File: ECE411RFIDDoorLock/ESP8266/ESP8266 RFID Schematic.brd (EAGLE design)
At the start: 61 x 43.8 mm, 30 parts, among them M1 SERVO, Q3 DMG341, T1 600mA/40V, T2 600mA/40V, U3 AP2112-3.3, X1 ESP-12E, X4 20329

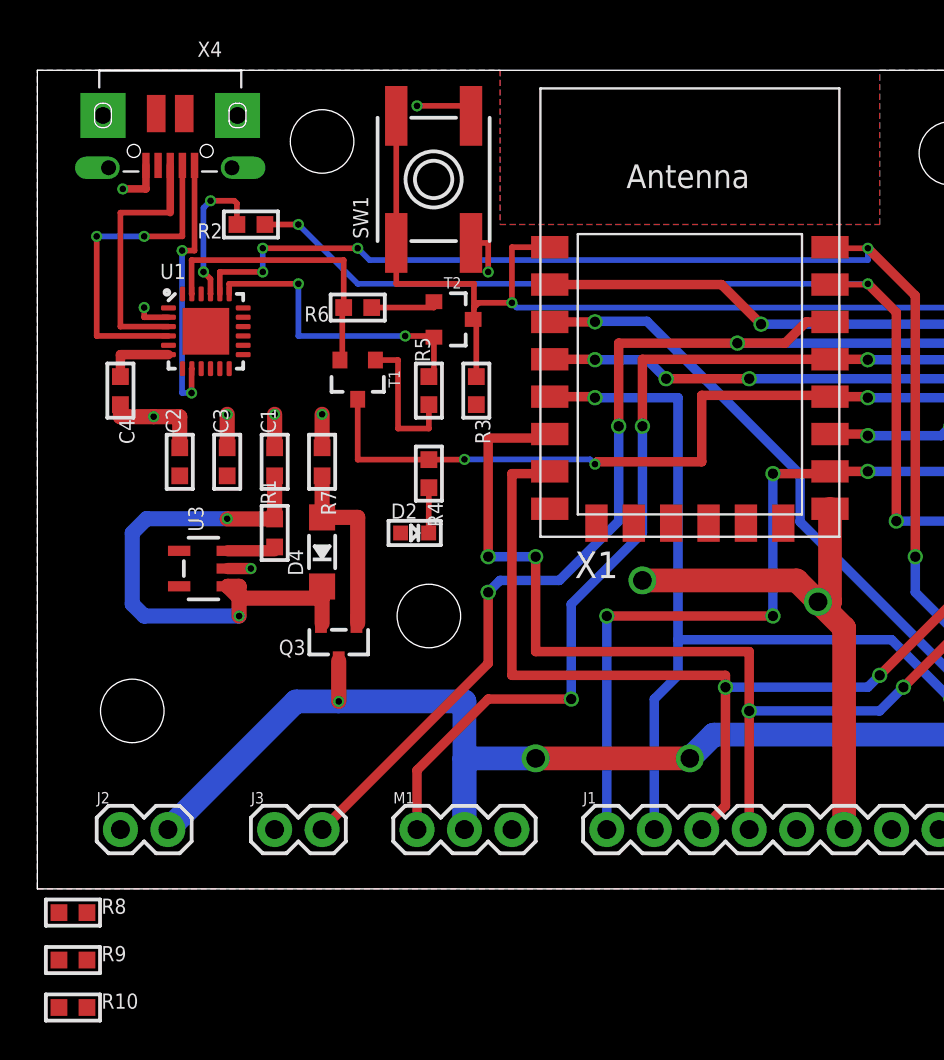
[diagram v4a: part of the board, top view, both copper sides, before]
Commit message: Added and routed resistors R8 - R10 that were missing from original schematic
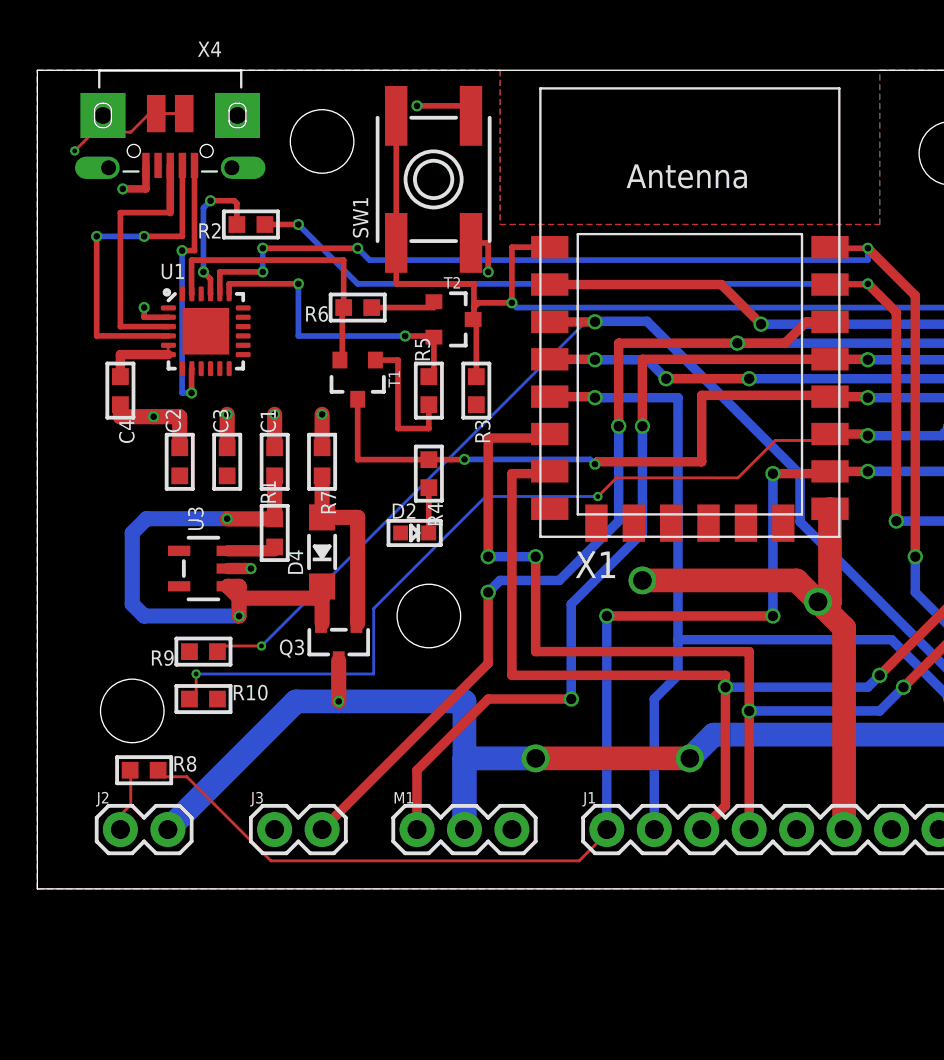
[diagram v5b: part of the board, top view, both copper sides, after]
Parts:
- moved R10 17.9 mm to (8.89, 10.2)
- moved R9 17.9 mm to (8.89, 12.7), turned to 180 degrees
- moved R8 8.52 mm to (5.71, 6.35)
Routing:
- net GPIO2: track 12.3 -> 55.1 mm, vias 2 -> 4
- net CH_PD: track 43.2 -> 70.7 mm, vias 1 -> 2
- net GPIO15: track 44.3 -> 71.3 mm
- net GND: track 50.6 -> 61.1 mm, vias 11 -> 12
- net N$14: track 3.75 -> 4.44 mm
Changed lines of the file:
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@@
 <autorouter>
 <pass name="Default">
-<param name="RoutingGrid" value="50mil"/>
+<param name="RoutingGrid" value="0.125mm"/>
 <param name="AutoGrid" value="1"/>
 <param name="Efforts" value="2"/>
 <param name="TopRouterVariant" value="1"/>
 <param name="tpViaShape" value="round"/>
-<param name="PrefDir.1" value="a"/>
+<param name="PrefDir.1" value="*"/>
 <param name="PrefDir.2" value="0"/>
 <param name="PrefDir.3" value="0"/>
@@
 <param name="PrefDir.14" value="0"/>
 <param name="PrefDir.15" value="0"/>
-<param name="PrefDir.16" value="a"/>
+<param name="PrefDir.16" value="-"/>
 <param name="cfVia" value="8"/>
 <param name="cfNonPref" value="5"/>
@@
 <attribute name="VALUE" x="9.89" y="45.907" size="0.4064" layer="27" ratio="10" rot="R180"/>
 </element>
-<element name="R8" library="microbuilder" package="0603-MINI" value="4.7k" x="1.905" y="-1.27" smashed="yes">
-<attribute name="NAME" x="3.429" y="-1.3335" size="0.8128" layer="25" ratio="18"/>
-<attribute name="VALUE" x="3.429" y="-1.905" size="0.4064" layer="27" ratio="10"/>
-</element>
-<element name="R9" library="microbuilder" package="0603-MINI" value="10k" x="1.905" y="-3.81" smashed="yes">
-<attribute name="NAME" x="3.429" y="-3.8735" size="0.8128" layer="25" ratio="18"/>
-<attribute name="VALUE" x="3.429" y="-4.445" size="0.4064" layer="27" ratio="10"/>
-</element>
-<element name="R10" library="microbuilder" package="0603-MINI" value="10k" x="1.905" y="-6.35" smashed="yes">
-<attribute name="NAME" x="3.429" y="-6.4135" size="0.8128" layer="25" ratio="18"/>
-<attribute name="VALUE" x="3.429" y="-6.985" size="0.4064" layer="27" ratio="10"/>
+<element name="R8" library="microbuilder" package="0603-MINI" value="4.7k" x="5.715" y="6.35" smashed="yes">
+<attribute name="NAME" x="7.239" y="6.2865" size="0.8128" layer="25" ratio="18"/>
+<attribute name="VALUE" x="7.239" y="5.715" size="0.4064" layer="27" ratio="10"/>
+</element>
+<element name="R9" library="microbuilder" package="0603-MINI" value="10k" x="8.89" y="12.7" smashed="yes" rot="R180">
+<attribute name="NAME" x="7.366" y="12.7635" size="0.8128" layer="25" ratio="18" rot="R180"/>
+<attribute name="VALUE" x="7.366" y="13.335" size="0.4064" layer="27" ratio="10" rot="R180"/>
+</element>
+<element name="R10" library="microbuilder" package="0603-MINI" value="10k" x="8.89" y="10.16" smashed="yes">
+<attribute name="NAME" x="10.414" y="10.0965" size="0.8128" layer="25" ratio="18"/>
+<attribute name="VALUE" x="10.414" y="9.525" size="0.4064" layer="27" ratio="10"/>
 </element>
 </elements>
@@
 </polygon>
 <contactref element="R8" pad="1"/>
-<wire x1="42.425" y1="20.345" x2="57.15" y2="33.655" width="0" layer="19" extent="1-1"/>
-<wire x1="25.4" y1="3.175" x2="32.385" y2="16.51" width="0" layer="19" extent="1-1"/>
-<wire x1="12.7" y1="3.175" x2="25.4" y2="3.175" width="0" layer="19" extent="1-1"/>
-<wire x1="4.445" y1="3.175" x2="12.7" y2="3.175" width="0" layer="19" extent="1-1"/>
-<wire x1="1.155" y1="-1.27" x2="4.445" y2="3.175" width="0" layer="19" extent="1-1"/>
-<wire x1="11.43" y1="17.145" x2="12.7" y2="3.175" width="0" layer="19" extent="1-1"/>
-<wire x1="10.16" y1="23.61" x2="10.1901" y2="17.145" width="0" layer="19" extent="1-1"/>
-<wire x1="12.7" y1="25.4" x2="10.16" y2="25.4" width="0" layer="19" extent="1-1"/>
-<wire x1="15.24" y1="25.4" x2="12.7" y2="25.4" width="0" layer="19" extent="1-1"/>
-<wire x1="7.62" y1="23.61" x2="10.16" y2="23.61" width="0" layer="19" extent="1-1"/>
-<wire x1="7.017" y1="30.595" x2="4.445" y2="25.92" width="0" layer="19" extent="1-1"/>
-<wire x1="4.572" y1="37.465" x2="5.715" y2="31.115" width="0" layer="19" extent="1-1"/>
-<wire x1="3.812" y1="38.597" x2="4.572" y2="37.465" width="0" layer="19" extent="1-1"/>
-<wire x1="6.362" y1="41.497" x2="5.812" y2="38.722" width="0" layer="19" extent="1-1"/>
-<wire x1="7.862" y1="41.497" x2="6.362" y2="41.497" width="0" layer="19" extent="1-1"/>
-<wire x1="3.512" y1="41.397" x2="3.812" y2="38.597" width="0" layer="19" extent="1-1"/>
-<wire x1="10.712" y1="41.397" x2="7.862" y2="41.497" width="0" layer="19" extent="1-1"/>
-<wire x1="10.412" y1="38.597" x2="10.712" y2="41.397" width="0" layer="19" extent="1-1"/>
-<wire x1="20.32" y1="41.91" x2="10.712" y2="41.397" width="0" layer="19" extent="1-1"/>
-<wire x1="23.209" y1="34.573" x2="23.209" y2="41.373" width="0" layer="19" extent="1-1"/>
+<wire x1="5" y1="4.5" x2="5" y2="6" width="0.1524" layer="1"/>
+<wire x1="4" y1="3.5" x2="5" y2="4.5" width="0.1524" layer="1"/>
+<wire x1="5" y1="6" x2="4.965" y2="6.35" width="0.1524" layer="1"/>
+<wire x1="4" y1="3.5" x2="4.445" y2="3.175" width="0.1524" layer="1"/>
+<wire x1="3" y1="40.5" x2="2" y2="39.5" width="0.1524" layer="1"/>
+<wire x1="5" y1="40.5" x2="3" y2="40.5" width="0.1524" layer="1"/>
+<wire x1="6" y1="41.5" x2="5" y2="40.5" width="0.1524" layer="1"/>
+<wire x1="6" y1="41.5" x2="6.362" y2="41.497" width="0.1524" layer="1"/>
+<wire x1="6.5" y1="41.5" x2="7.5" y2="41.5" width="0.1524" layer="1"/>
+<wire x1="7.5" y1="41.5" x2="7.862" y2="41.497" width="0.1524" layer="1"/>
+<wire x1="6.5" y1="41.5" x2="6.362" y2="41.497" width="0.1524" layer="1"/>
+<via x="2" y="39.5" extent="1-16" drill="0.254"/>
 </signal>
 <signal name="N$9">
@@
 <wire x1="50.045" y1="22.345" x2="53.975" y2="18.415" width="0.508" layer="16"/>
 <contactref element="R8" pad="2"/>
-<wire x1="2.655" y1="-1.27" x2="30.48" y2="3.175" width="0" layer="19" extent="1-1"/>
+<wire x1="8" y1="6" x2="6.5" y2="6" width="0.1524" layer="1"/>
+<wire x1="12.5" y1="1.5" x2="8" y2="6" width="0.1524" layer="1"/>
+<wire x1="29" y1="1.5" x2="12.5" y2="1.5" width="0.1524" layer="1"/>
+<wire x1="30.5" y1="3" x2="29" y2="1.5" width="0.1524" layer="1"/>
+<wire x1="6.5" y1="6" x2="6.465" y2="6.35" width="0.1524" layer="1"/>
+<wire x1="30.5" y1="3" x2="30.48" y2="3.175" width="0.1524" layer="1"/>
 </signal>
 <signal name="GPIO0">
@@
 <wire x1="50.165" y1="26.035" x2="53.975" y2="26.035" width="0.508" layer="1"/>
 <contactref element="R10" pad="1"/>
-<wire x1="1.155" y1="-6.35" x2="42.425" y2="24.345" width="0" layer="19" extent="1-1"/>
+<wire x1="8.5" y1="11.5" x2="8.5" y2="10.5" width="0.1524" layer="1"/>
+<wire x1="18" y1="11.5" x2="8.5" y2="11.5" width="0.1524" layer="16"/>
+<wire x1="18" y1="15" x2="18" y2="11.5" width="0.1524" layer="16"/>
+<wire x1="24" y1="21" x2="18" y2="15" width="0.1524" layer="16"/>
+<wire x1="30" y1="21" x2="24" y2="21" width="0.1524" layer="16"/>
+<wire x1="31" y1="22" x2="30" y2="21" width="0.1524" layer="1"/>
+<wire x1="37.5" y1="22" x2="31" y2="22" width="0.1524" layer="1"/>
+<wire x1="39.5" y1="24" x2="37.5" y2="22" width="0.1524" layer="1"/>
+<wire x1="42" y1="24" x2="39.5" y2="24" width="0.1524" layer="1"/>
+<wire x1="8.5" y1="10.5" x2="8.14" y2="10.16" width="0.1524" layer="1"/>
+<wire x1="42" y1="24" x2="42.425" y2="24.345" width="0.1524" layer="1"/>
+<via x="8.5" y="11.5" extent="1-16" drill="0.254"/>
+<via x="30" y="21" extent="1-16" drill="0.254"/>
 </signal>
 <signal name="GPIO5/SCL">
@@
 <wire x1="32.6287" y1="30.3784" x2="40.8239" y2="22.1832" width="0.508" layer="16"/>
 <contactref element="R9" pad="1"/>
-<wire x1="1.155" y1="-3.81" x2="27.425" y2="30.345" width="0" layer="19" extent="1-1"/>
+<wire x1="12" y1="13" x2="10" y2="13" width="0.1524" layer="1"/>
+<wire x1="29.5" y1="30.5" x2="12" y2="13" width="0.1524" layer="16"/>
+<wire x1="10" y1="13" x2="9.64" y2="12.7" width="0.1524" layer="1"/>
+<wire x1="29.5" y1="30.5" x2="29.845" y2="30.353" width="0.1524" layer="16"/>
+<via x="12" y="13" extent="1-16" drill="0.254"/>
 </signal>
 <signal name="USB_RX">
@@
 <contactref element="R9" pad="2"/>
 <contactref element="R10" pad="2"/>
-<wire x1="27.425" y1="20.345" x2="57.15" y2="38.735" width="0" layer="19" extent="1-1"/>
-<wire x1="23.495" y1="25.92" x2="27.425" y2="20.345" width="0" layer="19" extent="1-1"/>
-<wire x1="19.443" y1="19.05" x2="23.495" y2="25.92" width="0" layer="19" extent="1-1"/>
-<wire x1="10.16" y1="22.11" x2="19.443" y2="19.05" width="0" layer="19" extent="1-1"/>
-<wire x1="7.62" y1="22.11" x2="10.16" y2="22.11" width="0" layer="19" extent="1-1"/>
-<wire x1="7.767" y1="27.845" x2="7.62" y2="22.11" width="0" layer="19" extent="1-1"/>
-<wire x1="7.5899" y1="16.195" x2="7.62" y2="22.11" width="0" layer="19" extent="1-1"/>
-<wire x1="2.655" y1="-3.81" x2="7.5899" y2="16.195" width="0" layer="19" extent="1-1"/>
-<wire x1="2.655" y1="-6.35" x2="2.655" y2="-3.81" width="0" layer="19" extent="1-1"/>
-<wire x1="48.26" y1="3.175" x2="27.425" y2="20.345" width="0" layer="19" extent="1-1"/>
 </signal>
 <signal name="N$2">
@@
 <wire x1="4.445" y1="27.42" x2="4.445" y2="28.595" width="0.508" layer="1"/>
 <wire x1="4.445" y1="28.595" x2="7.017" y2="28.595" width="0.508" layer="1"/>
-<wire x1="7.017" y1="28.595" x2="7.017" y2="29.095" width="0" layer="19" extent="1-1"/>
+<wire x1="7" y1="28.5" x2="7" y2="29" width="0.1524" layer="1"/>
+<wire x1="7" y1="29" x2="7.017" y2="29.095" width="0.1524" layer="1"/>
+<wire x1="7" y1="28.5" x2="7.017" y2="28.595" width="0.1524" layer="1"/>
 </signal>
 <signal name="EN">

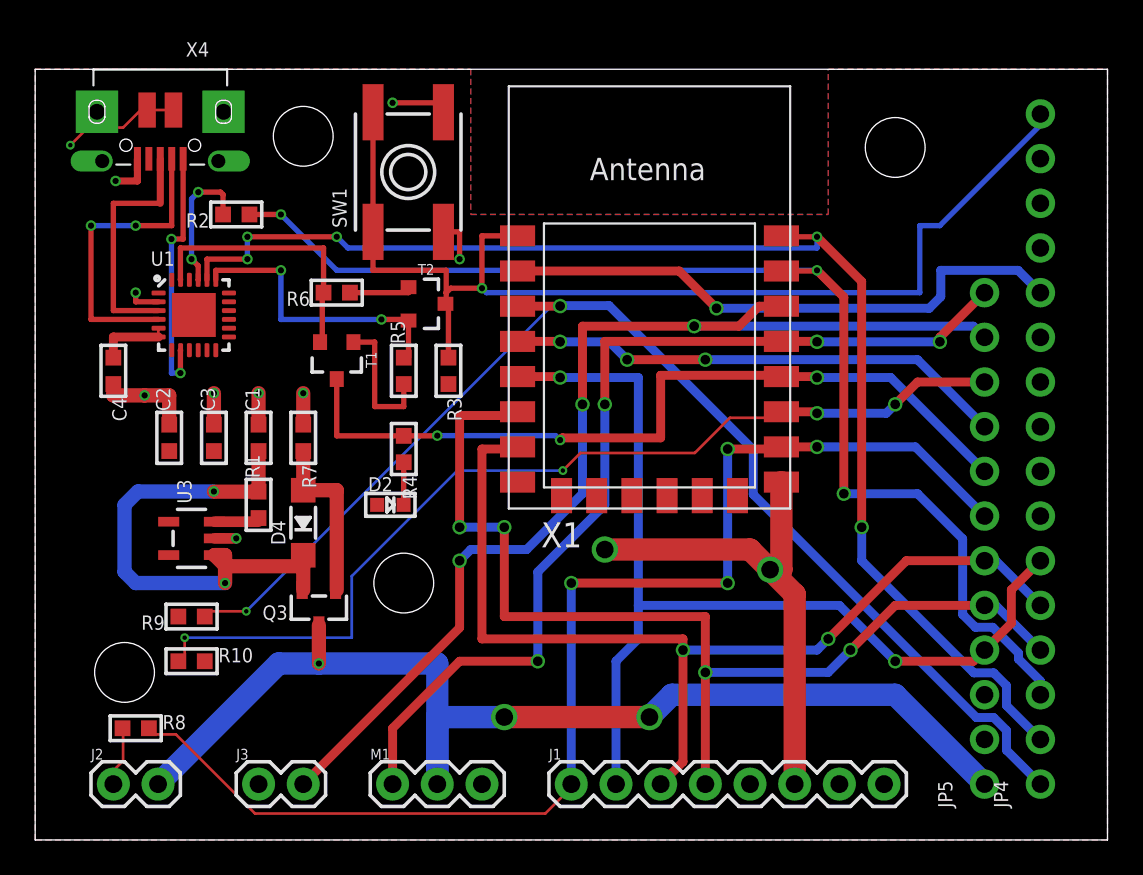
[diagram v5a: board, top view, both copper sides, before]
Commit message: cleaned up some of the errors. Need to route 3.3V
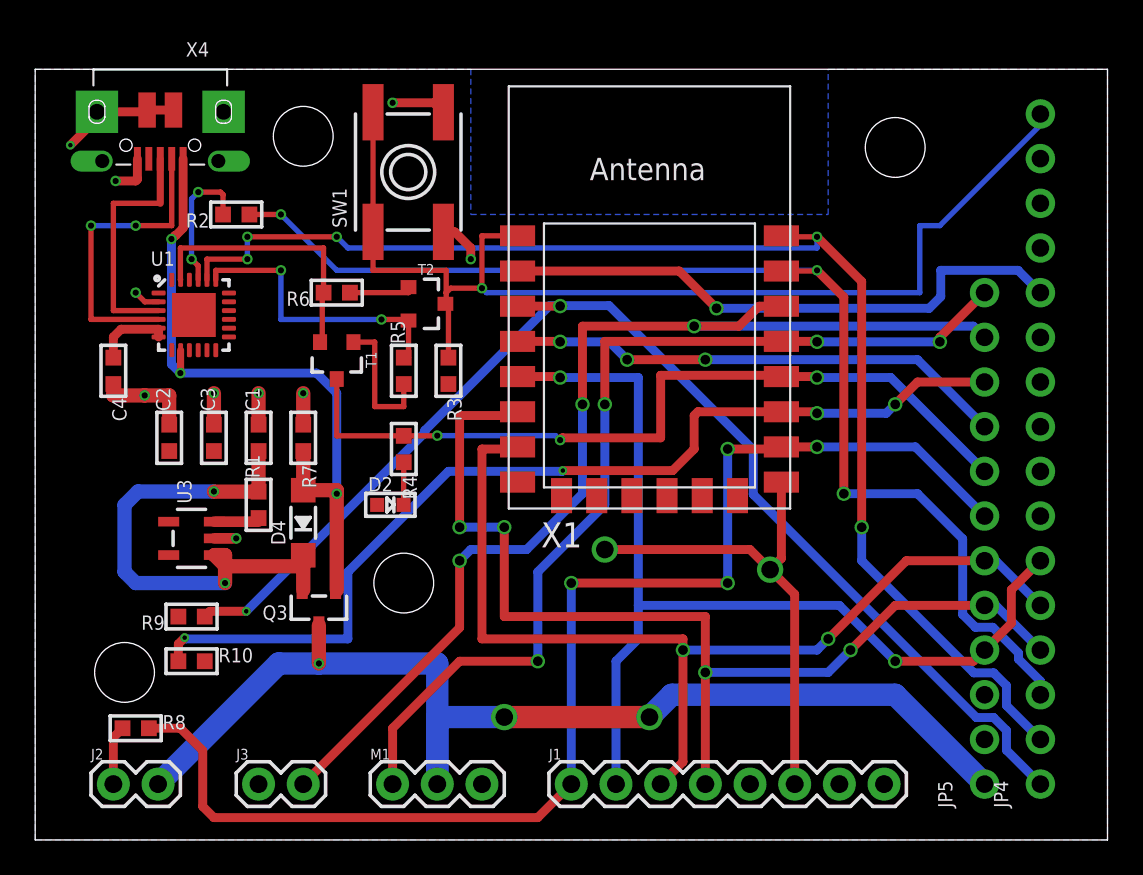
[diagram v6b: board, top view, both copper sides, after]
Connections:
- removed net N$2: U1.8, X4.VBUS
- removed net N$9: D4.A, Q3.1, R7.2
- net 3.3V: no longer U1.7
- net VBUS: now also D4.A, Q3.1, R7.2, U1.7, U1.8, X4.VBUS
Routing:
- net VBUS: track 0.00 -> 38.9 mm, vias 0 -> 3
- net N$2: track 14.7 -> 0.00 mm, vias 2 -> 0
- net N$9: track 9.87 -> 0.00 mm
- net GPIO15: track 71.3 -> 73.1 mm
- net GPIO2: track 55.1 -> 56.5 mm
- net GND: track 61.1 -> 59.9 mm
- removed copper zone on layer 1, net 3.3V

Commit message: Two ground planes, clean up, and power routing
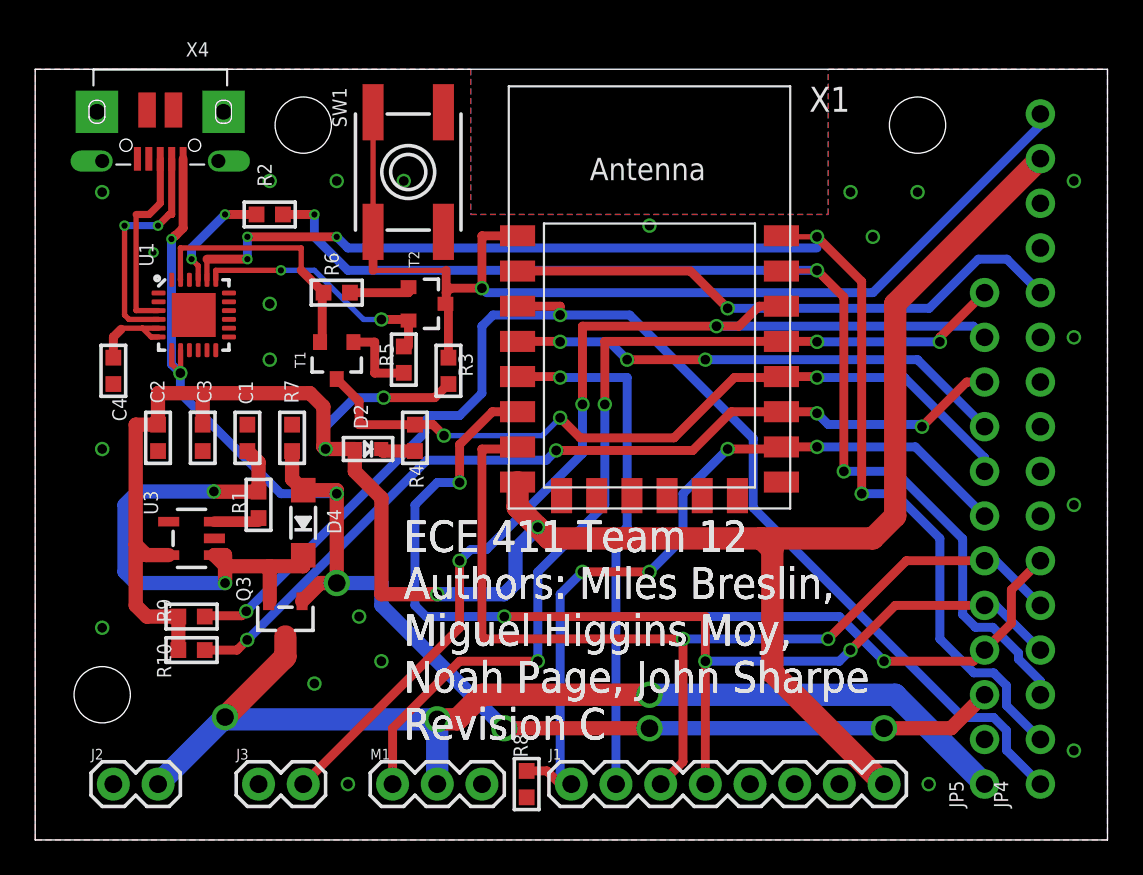
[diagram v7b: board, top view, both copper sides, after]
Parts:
- moved R8 22.5 mm to (27.9, 3.17), turned to 90 degrees
- moved D2 3.42 mm to (18.9, 22.2)
- moved Q3 2.01 mm to (14.2, 12.6)
- moved R2 1.91 mm to (13.3, 35.6)
- moved R4 0.90 mm to (21.6, 22.9)
- moved C1 0.63 mm to (12.1, 22.9)
- moved C2 0.63 mm to (6.99, 22.9), turned to 270 degrees
- moved C3 0.63 mm to (9.53, 22.9), turned to 270 degrees
- moved R10 0.63 mm to (8.89, 10.8), turned to 180 degrees
- moved R7 0.63 mm to (14.6, 22.9)
- moved R5 0.63 mm to (21.0, 27.3)
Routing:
- net 3.3V: track 0.00 -> 130.2 mm, vias 0 -> 4
- net GND: track 59.9 -> 0.00 mm, vias 12 -> 1
- net VBUS: track 38.9 -> 81.8 mm, vias 3 -> 7
- net GPIO15: track 73.1 -> 44.7 mm
- net GPIO2: track 56.5 -> 51.4 mm
- net N$4: track 17.6 -> 13.2 mm
- net VBAT: track 65.3 -> 61.0 mm
- net CH_PD: track 70.8 -> 74.2 mm
- net N$6: track 7.81 -> 4.63 mm
- net N$3: track 13.9 -> 10.9 mm
- net GPIO5/SCL: track 63.0 -> 60.4 mm
- net GPIO12/MISO: track 60.1 -> 62.7 mm
- net RTS: track 16.7 -> 14.5 mm
- net RESET: track 64.1 -> 61.9 mm
- net GPIO0: track 46.0 -> 44.1 mm
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- added copper zone on layer 1, net GND
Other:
- board text added: "ECE 411 Team 12 Authors: Miles Breslin, Miguel Higgins Moy, Noah Page, John Sharpe Revision C"
